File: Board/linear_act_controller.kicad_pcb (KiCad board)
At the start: 4 copper layers, 90 x 40 mm, 79 parts, among them J1 SSV, J2 PWR_LED, J3 STATUS_LED, J4 ACTUATOR, J5 PROG, Q1 IRLML6344TRPBF, U1 MP6612, U2 LMR51635XDDCR, U3 STM32F030K6Tx, U4 MP2459

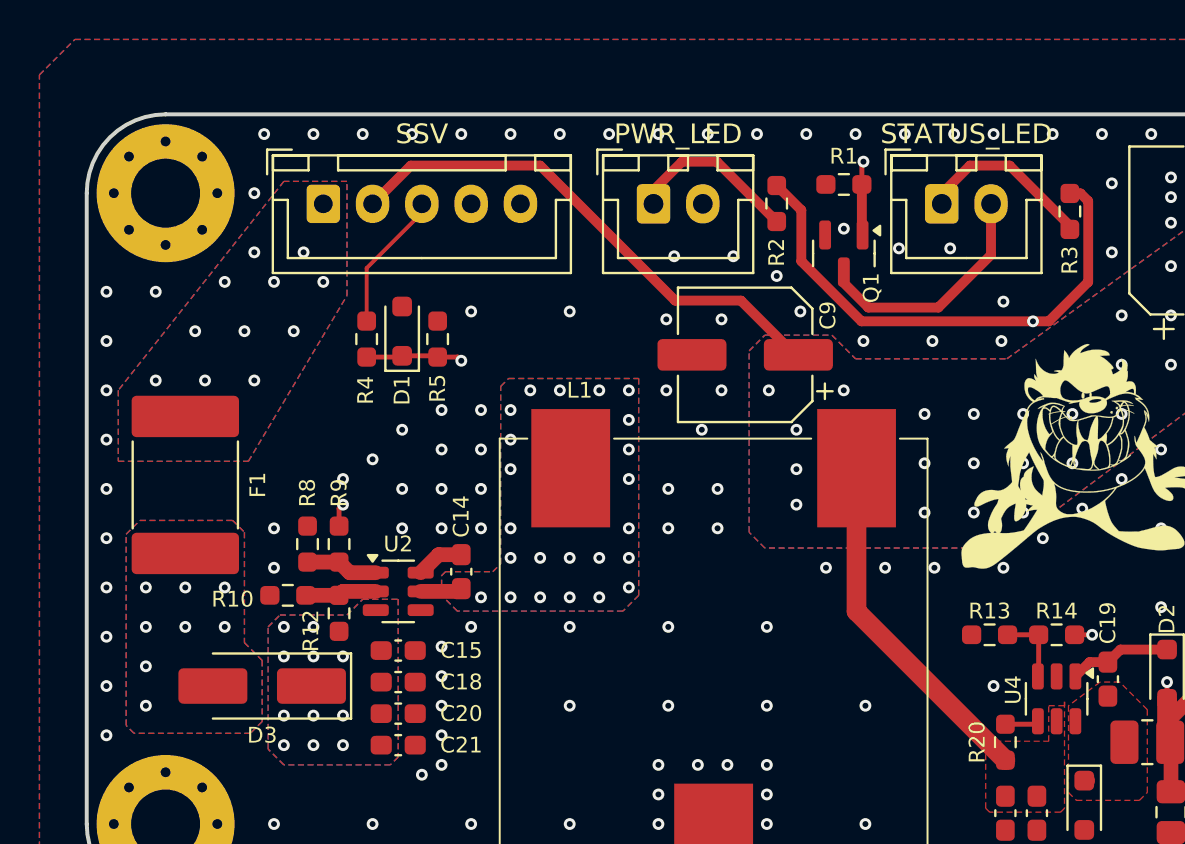
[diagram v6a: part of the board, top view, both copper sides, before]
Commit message: Split "SSV" connector into "PWR" and "CONTROL"
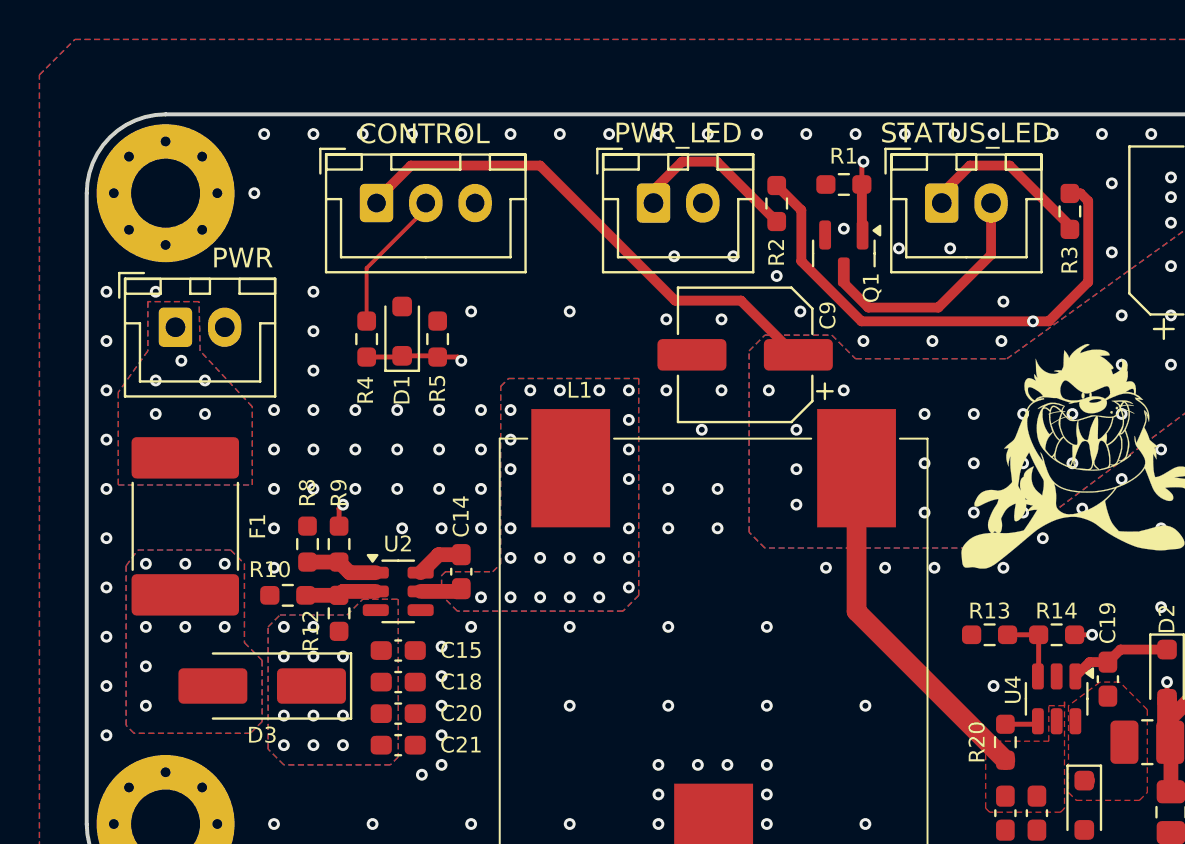
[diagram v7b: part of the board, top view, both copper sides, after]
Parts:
- added J8: CONTROL, Connector_JST:JST_XH_B3B-XH-A_1x03_P2.50mm_Vertical, F.Cu at (69.7, 84.5)
- J1: value SSV -> PWR; footprint Connector_JST:JST_XH_B5B-XH-A_1x05_P2.50mm_Vertical -> Connector_JST:JST_XH_B2B-XH-A_1x02_P2.50mm_Vertical
- moved J1 9.77 mm to (59.5, 90.8)
- moved F1 2.10 mm to (60.0, 100.9)
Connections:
- J1 pad 2: +24V -> GND
- R4 pad 1: Net-(J1-Pin_3) -> Net-(J8-Pin_2)
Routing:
- net Net-(J8-Pin_2): track 0.00 -> 7.11 mm
- net Net-(J1-Pin_3): track 7.11 -> 0.00 mm
- net VIN: vias 11 -> 5
- net GND: vias 205 -> 216

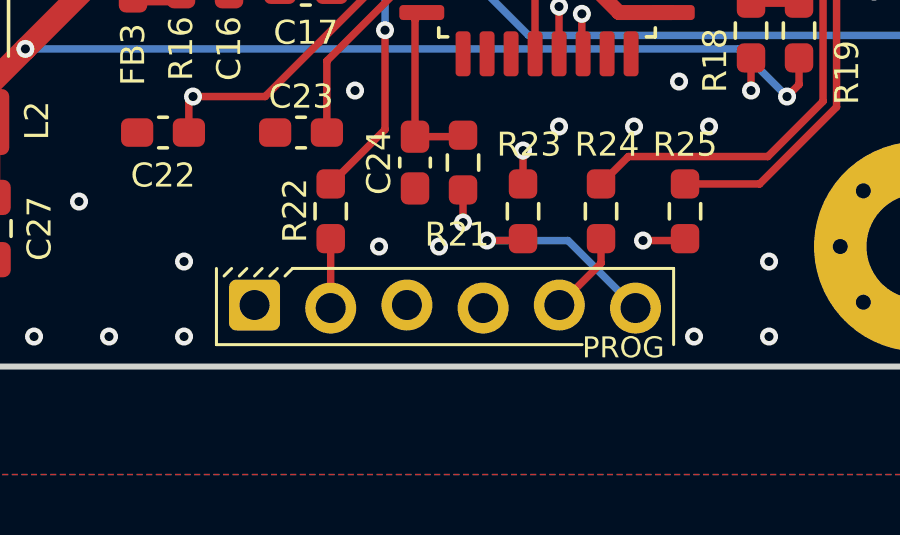
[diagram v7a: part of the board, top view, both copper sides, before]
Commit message: Updated prog header with increased dealignment
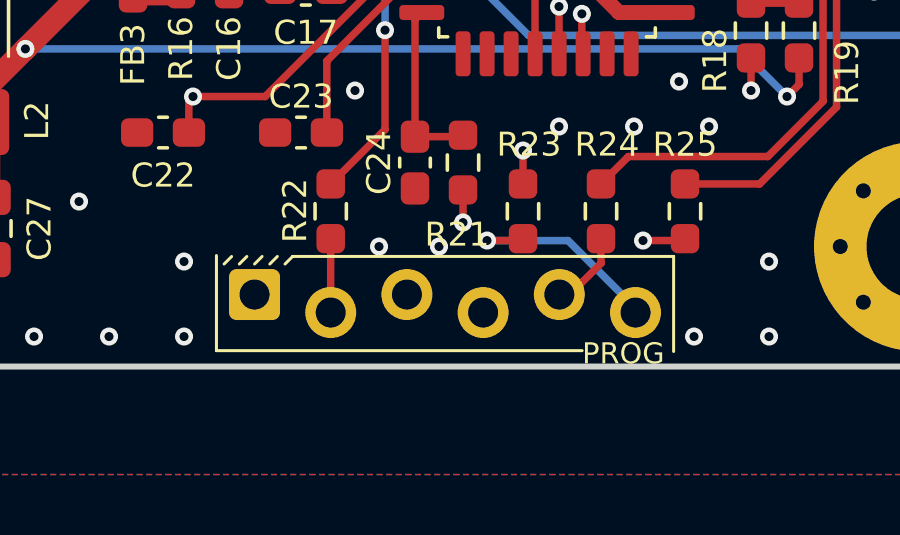
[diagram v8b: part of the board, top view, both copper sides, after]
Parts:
- moved J5 0.10 mm to (118.8, 117.9)
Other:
- board text added: "Linear actuator controller revA.1 https://github.com/Talw3g/linear_act_controller"
- board text removed: "Linear actuator controller revA https://github.com/Talw3g/linear_act_controller"
